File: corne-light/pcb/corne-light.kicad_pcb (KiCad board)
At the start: 2 copper layers, 275.5 x 105.6 mm, 122 parts, among them J1 MJ-4PP-9, J2 OLED, J5 Breakaway_Tabs, J6 MJ-4PP-9, J7 OLED, SW1 SW_PUSH, SW10 SW_PUSH, SW11 SW_PUSH, SW12 SW_PUSH, SW13 SW_PUSH, SW14 SW_PUSH, SW15 SW_PUSH, SW16 SW_PUSH, SW17 SW_PUSH, SW18 SW_PUSH, SW19 SW_PUSH, SW2 SW_PUSH, SW20 SW_PUSH, SW21 SW_PUSH, SW22 SW_PUSH, SW23 SW_PUSH, SW24 SW_PUSH, SW25 SW_PUSH, SW26 SW_PUSH, SW27 SW_PUSH, SW28 SW_PUSH, SW29 SW_PUSH, SW3 SW_PUSH, SW30 SW_PUSH, SW31 SW_PUSH, SW32 SW_PUSH, SW33 SW_PUSH, SW34 SW_PUSH, SW35 SW_PUSH, SW36 SW_PUSH, SW37 SW_PUSH, SW38 SW_PUSH, SW39 SW_PUSH, SW4 SW_PUSH, SW40 SW_PUSH, SW41 SW_PUSH, SW42 SW_PUSH, SW5 SW_PUSH, SW6 SW_PUSH, SW7 SW_PUSH, SW8 SW_PUSH, SW9 SW_PUSH, U1 ProMicro, U2 ProMicro

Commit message: Remove breakoff cutouts for corne-light
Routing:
- net row2_r: track 137.6 -> 127.3 mm
- net row2: track 153.9 -> 143.8 mm
- net row0_r: track 127.8 -> 121.5 mm
- net row1_r: track 134.3 -> 128.0 mm
- net row1: track 164.0 -> 157.7 mm
- net row0: track 142.3 -> 136.1 mm
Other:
- outline, holes or cut-outs redrawn

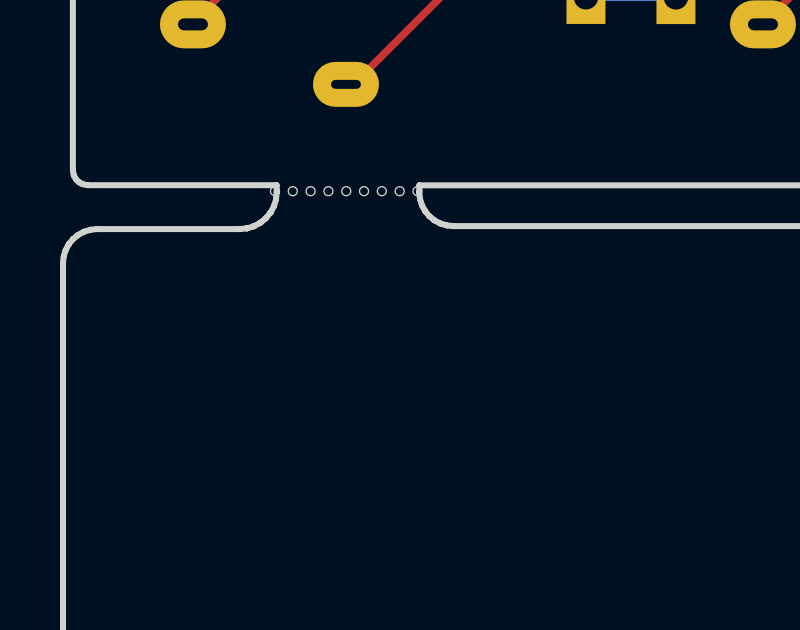
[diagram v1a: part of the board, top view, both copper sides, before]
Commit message: Add JLC order number placeholder
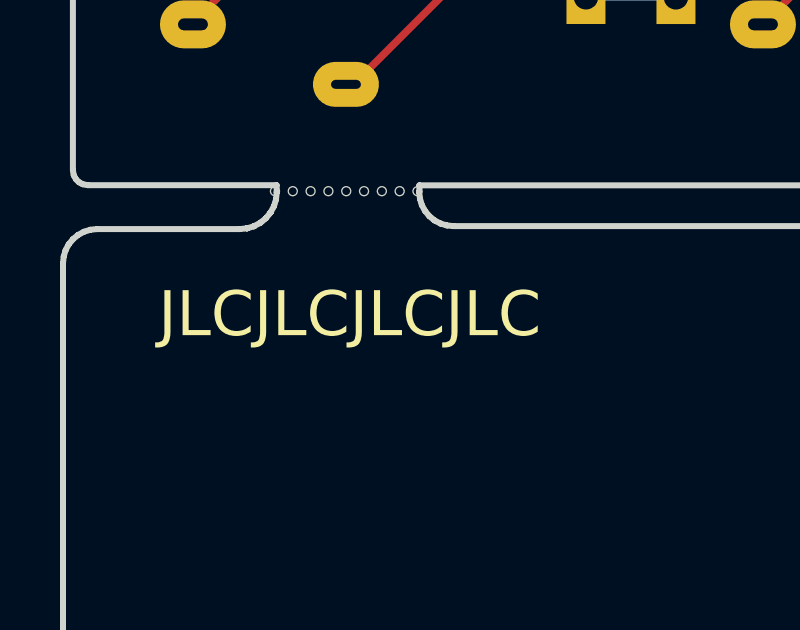
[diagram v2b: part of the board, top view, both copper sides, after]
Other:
- board text added: "JLCJLCJLCJLC"
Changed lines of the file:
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@@
   (general
     (thickness 1.6)
-    (drawings 741)
+    (drawings 743)
     (tracks 1212)
     (zones 0)
@@
     (pad "" np_thru_hole circle (at 0 0) (size 0.3 0.3) (drill 0.3) (layers *.Cu *.Mask))
   )
+  (gr_text JLCJLCJLCJLC (at 22.2225 97.485) (layer B.SilkS)
+    (effects (font (size 1.5 1.5) (thickness 0.3)) (justify mirror))
+  )
+  (gr_text JLCJLCJLCJLC (at 22.3125 97.485) (layer F.SilkS)
+    (effects (font (size 1.5 1.5) (thickness 0.3)))
+  )
   (gr_line (start 50.583768 36.929478) (end 13.6975 36.929478) (layer Edge.Cuts) (width 0.2))
